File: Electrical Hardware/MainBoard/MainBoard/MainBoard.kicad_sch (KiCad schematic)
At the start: 76 parts, among them J1 SM02B-SRSS-TB_LFSN_, J2 Conn_01x04_Socket, J3 Conn_01x04_Socket, J4 Conn_01x04_Socket, J5 USB_B_Micro, J6 Thermistor, J7 62684-401100ALF, J8 Conn_01x02_Socket, SW1 SW_Push, SW2 SW_Push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

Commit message: Add potential new USB C port; make minor layout edits
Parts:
- added J9: 1054550101, 105455-0101_MOL, symbol 1054550101:1054550101
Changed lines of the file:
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@@
+    )
+  )
+  (symbol (lib_id "1054550101:1054550101") (at 191.77 172.72 0) (unit 1)
+    (in_bom yes) (on_board yes) (dnp no) (fields_autoplaced)
+    (property "Reference" "J9" (at 212.09 162.56 0)
+      (effects (font (size 1.524 1.524)))
+    )
+    (property "Value" "1054550101" (at 212.09 165.1 0)
+      (effects (font (size 1.524 1.524)))
+    )
+    (property "Footprint" "105455-0101_MOL" (at 191.77 172.72 0)
+      (effects (font (size 1.27 1.27) italic) hide)
+    )
+    (property "Datasheet" "1054550101" (at 191.77 172.72 0)
+      (effects (font (size 1.27 1.27) italic) hide)
+    )
+    (pin "25")
+    (pin "26")
+    (pin "27")
+    (pin "28")
+    (pin "A1")
+    (pin "A10")
+    (pin "A11")
+    (pin "A12")
+    (pin "A2")
+    (pin "A3")
+    (pin "A4")
+    (pin "A5")
+    (pin "A6")
+    (pin "A7")
+    (pin "A8")
+    (pin "A9")
+    (pin "B1")
+    (pin "B10")
+    (pin "B11")
+    (pin "B12")
+    (pin "B2")
+    (pin "B3")
+    (pin "B4")
+    (pin "B5")
+    (pin "B6")
+    (pin "B7")
+    (pin "B8")
+    (pin "B9")
+    (instances
+      (project "MainBoard"
+        (path "/962ff572-1dde-45a8-8fb2-b4e07b12aec2"
+          (reference "J9") (unit 1)
+        )
+      )
     )
   )

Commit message: Add another potential USB-C with simplified pinout
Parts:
- added J10: UJC-HP-M-G-5-MSMT-TR, UJC_HP_M_G_5_MSMT_TR:CUI_UJC-HP-M-G-5-MSMT-TR, symbol UJC_HP_M_G_5_MSMT_TR:UJC-HP-M-G-5-MSMT-TR
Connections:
- net GND: now also J9.25 (GND), J9.26 (GND), J9.27 (GND), J9.28 (GND), J9.A1 (GND), J9.A12 (GND), J9.B1 (GND), J9.B12 (GND), J10.A12 (GND), J10.B12 (GND__1)

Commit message: Add yet another USB-C, this time's the charm - simplified pinout but still for comms
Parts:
- added J11: USB4500-03-0-A_REVA1, USB4500-03-0-A:GCT_USB4500-03-0-A_REVA1, symbol USB4500-03-0-A:USB4500-03-0-A_REVA1
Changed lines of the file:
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@@
+    )
+  )
+  (symbol (lib_id "USB4500-03-0-A:USB4500-03-0-A_REVA1") (at 210.82 248.92 0) (unit 1)
+    (in_bom yes) (on_board yes) (dnp no) (fields_autoplaced)
+    (property "Reference" "J11" (at 210.82 228.6 0)
+      (effects (font (size 1.27 1.27)))
+    )
+    (property "Value" "USB4500-03-0-A_REVA1" (at 210.82 231.14 0)
+      (effects (font (size 1.27 1.27)))
+    )
+    (property "Footprint" "USB4500-03-0-A:GCT_USB4500-03-0-A_REVA1" (at 210.82 248.92 0)
+      (effects (font (size 1.27 1.27)) (justify bottom) hide)
+    )
+    (property "Datasheet" "" (at 210.82 248.92 0)
+      (effects (font (size 1.27 1.27)) hide)
+    )
+    (property "PARTREV" "A1" (at 210.82 248.92 0)
+      (effects (font (size 1.27 1.27)) (justify bottom) hide)
+    )
+    (property "STANDARD" "Manufacturer Recommendations" (at 210.82 248.92 0)
+      (effects (font (size 1.27 1.27)) (justify bottom) hide)
+    )
+    (property "SNAPEDA_PN" "USB4500-03-0-A" (at 210.82 248.92 0)
+      (effects (font (size 1.27 1.27)) (justify bottom) hide)
+    )
+    (property "MAXIMUM_PACKAGE_HEIGHT" "2.36 mm" (at 210.82 248.92 0)
+      (effects (font (size 1.27 1.27)) (justify bottom) hide)
+    )
+    (property "MANUFACTURER" "Global Connector Technology" (at 210.82 248.92 0)
+      (effects (font (size 1.27 1.27)) (justify bottom) hide)
+    )
+    (pin "A1_B12")
+    (pin "A4_B9")
+    (pin "A5")
+    (pin "A6")
+    (pin "A7")
+    (pin "A8")
+    (pin "B1_A12")
+    (pin "B4_A9")
+    (pin "B5")
+    (pin "B6")
+    (pin "B7")
+    (pin "B8")
+    (pin "SH1")
+    (pin "SH2")
+    (pin "SH3")
+    (pin "SH4")
+    (instances
+      (project "MainBoard"
+        (path "/962ff572-1dde-45a8-8fb2-b4e07b12aec2"
+          (reference "J11") (unit 1)
+        )
+      )
     )
   )

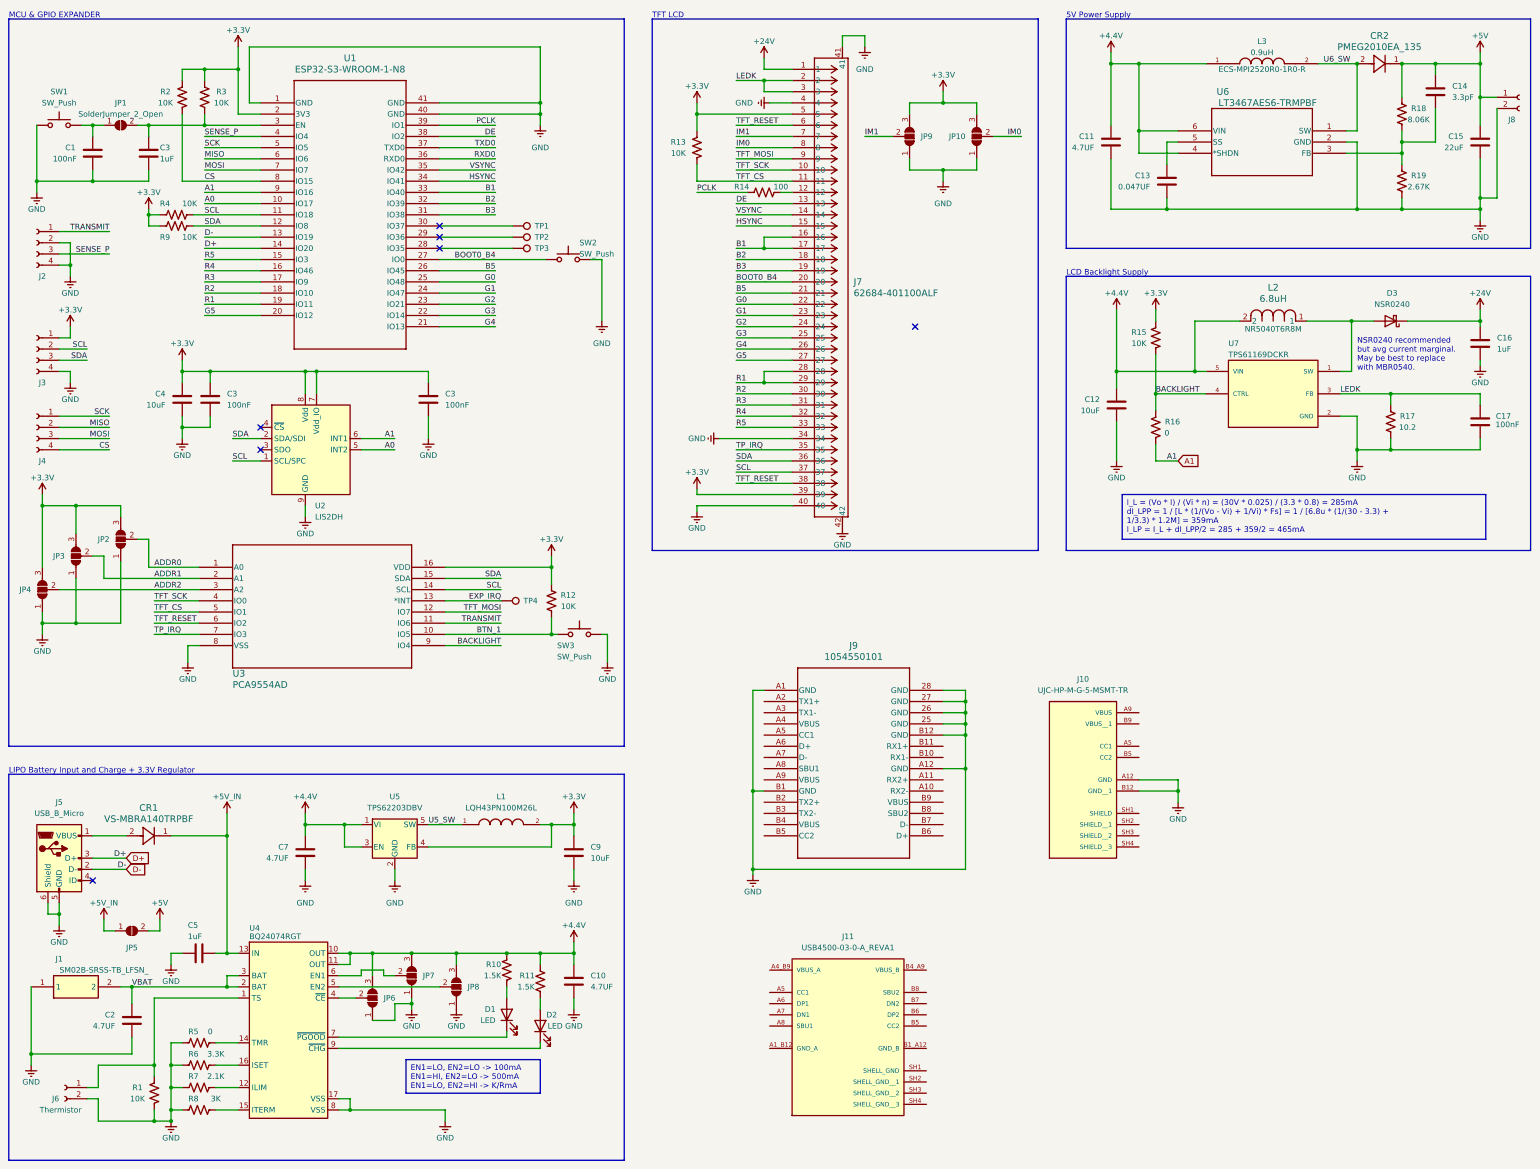
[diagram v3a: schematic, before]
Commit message: Settle USB-C schematic update; begin USB-C layout edits
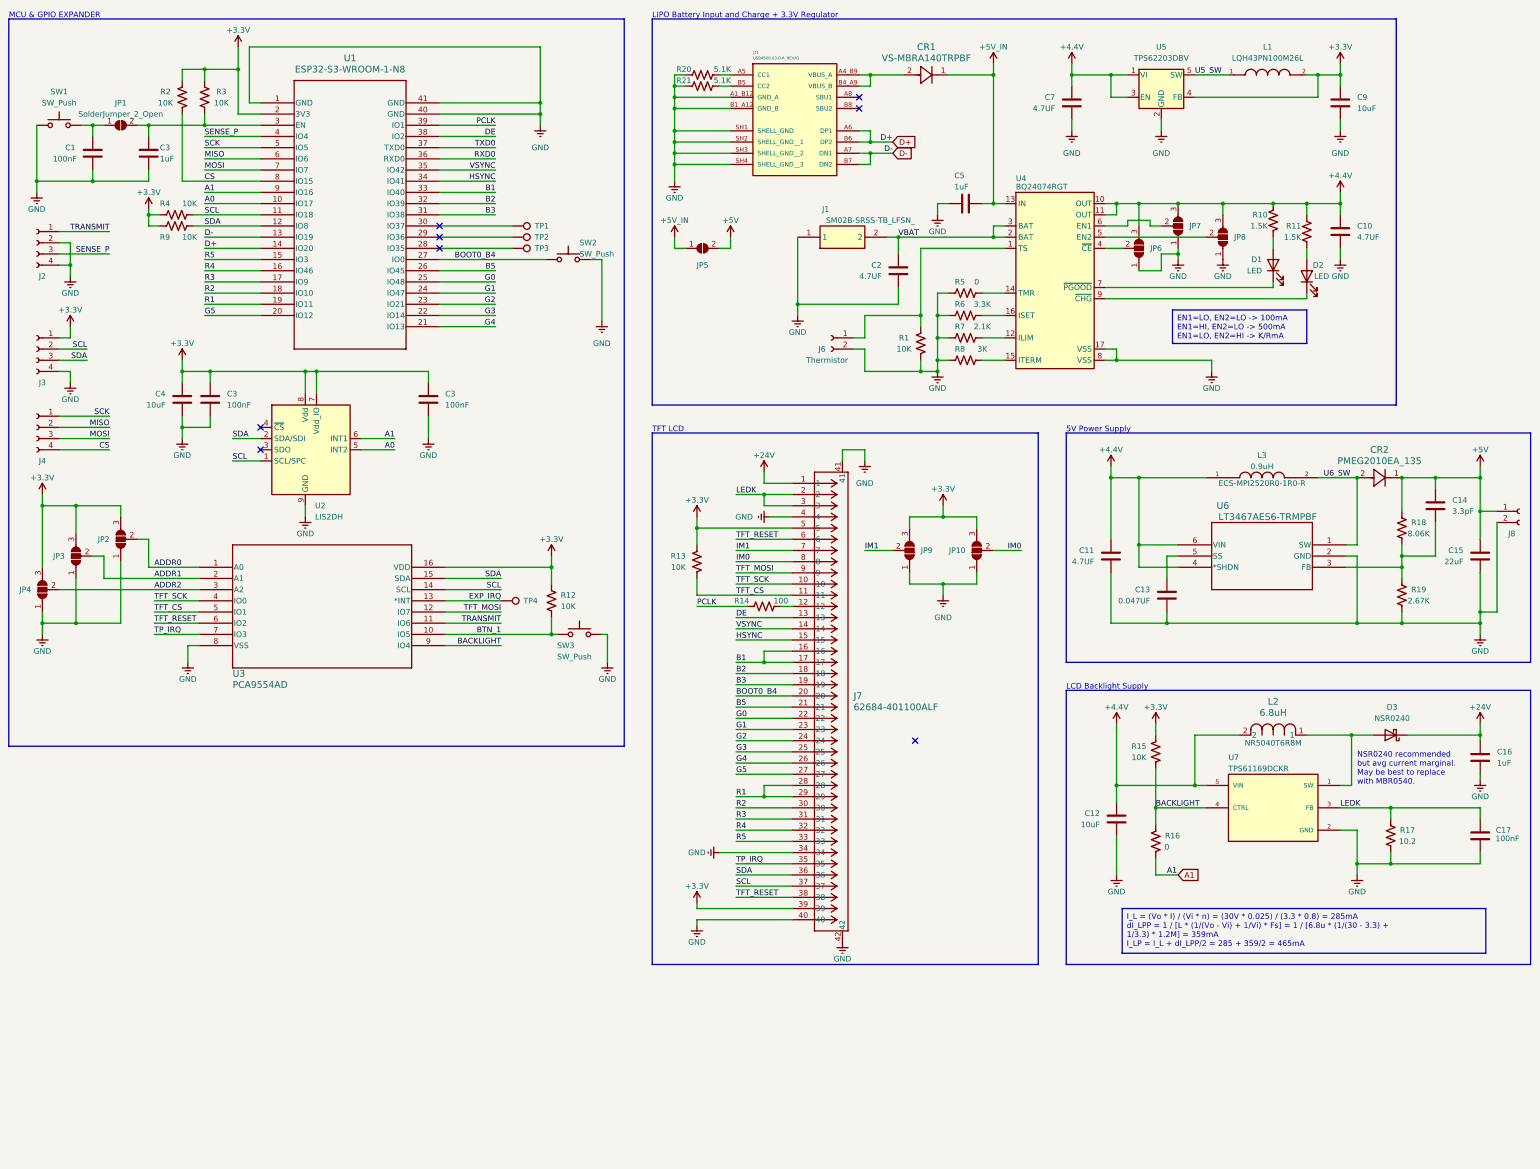
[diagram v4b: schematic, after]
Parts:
- removed J10: UJC-HP-M-G-5-MSMT-TR, UJC_HP_M_G_5_MSMT_TR:CUI_UJC-HP-M-G-5-MSMT-TR, symbol UJC_HP_M_G_5_MSMT_TR:UJC-HP-M-G-5-MSMT-TR
- removed J5: USB_B_Micro, Connector_USB:USB_Micro-B_Amphenol_10118193-0001LF_Horizontal, symbol Connector:USB_B_Micro
- removed J9: 1054550101, 105455-0101_MOL, symbol 1054550101:1054550101
- added R20, R21: 5.1K, Resistor_SMD:R_0603_1608Metric, symbol Device:R_US
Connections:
- net D+: now also J11.A6 (DP1), J11.B6 (DP2)
- net D-: now also J11.A7 (DN1), J11.B7 (DN2)
- net GND: now also J11.A1_B12 (GND_A), J11.B1_A12 (GND_B), J11.SH1 (SHELL_GND), J11.SH2 (SHELL_GND__1), J11.SH3 (SHELL_GND__2), J11.SH4 (SHELL_GND__3), R20.2, R21.2
- net at J11.A4_B9 (VBUS_A): now also CR1.2, J11.B4_A9 (VBUS_B)
- net at J11.A5 (CC1): now also R20.1
- net at J11.B5 (CC2): now also R21.1
- no-connect marks 7 -> 8
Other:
- moved on the sheet: C10, C11, C12, C13, C14, C15, C16, C17, C2, C5, C7, C9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

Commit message: Add smaller gpio expander footprint
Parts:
- U3: footprint SOT162-1_NXP -> PCA9554AD:SOT338-1_NXP-L
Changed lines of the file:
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@@
       (effects (font (size 1.524 1.524)) (justify left))
     )
-    (property "Footprint" "SOT162-1_NXP" (at 63.5 144.78 0)
+    (property "Footprint" "PCA9554AD:SOT338-1_NXP-L" (at 63.5 144.78 0)
       (effects (font (size 1.27 1.27) italic) hide)
     )
